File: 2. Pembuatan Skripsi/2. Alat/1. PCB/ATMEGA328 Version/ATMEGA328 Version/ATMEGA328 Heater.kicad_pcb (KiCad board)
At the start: 2 copper layers, 52.3 x 63.6 mm, 64 parts, among them J1 Conn_01x02, J2 Sensors, J3 Screw_Terminal_01x02, J5 FTDI, J6 Conn_02x04_Top_Bottom, K1 EE2-4.5NU, Q1 S9013, Q2 S9013, Q3 S9013, Q4 MMBT2222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

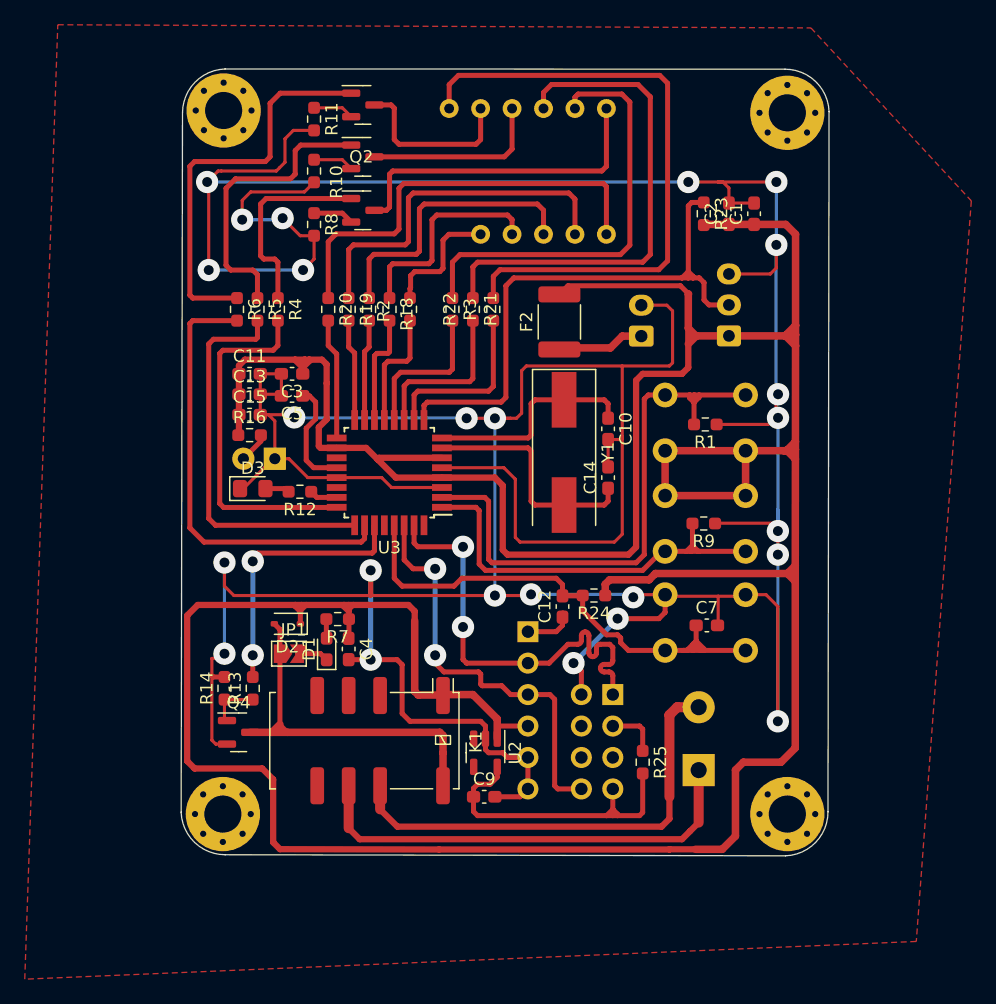
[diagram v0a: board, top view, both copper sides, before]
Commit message: Huge update for ATMEGA328P Board
Program is fully working:

- Get parameter, sensor data, led status, relay status.
- Show parameter on SevSeg
- Connected to NodeRed
- Board design is revised based on actual board
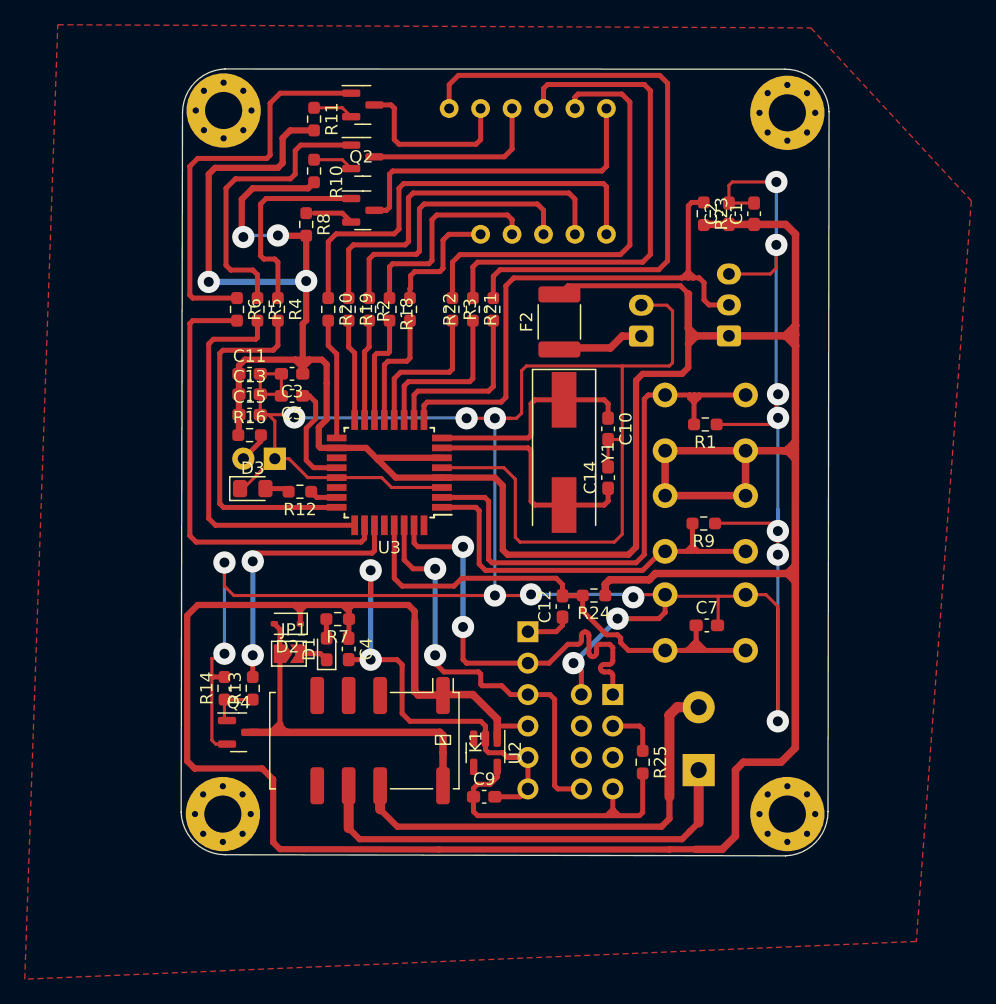
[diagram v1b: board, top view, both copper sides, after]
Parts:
- R10, R8: value 100 -> 1K
- R11: value 100 -> 1k
- R17, R18, R19, R20, R21, R22, R3: value 1K -> 510
- R23: value 10K -> 4K7
- moved R8 0.63 mm to (64.5, 75.6)
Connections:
- R10 pad 2: GND -> VCC
- R11 pad 2: GND -> VCC
- R5 pad 1: Net-(Q2-B) -> EN2
- R5 pad 2: EN2 -> Net-(Q2-B)
- R8 pad 2: GND -> VCC
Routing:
- net GND: track 411.5 -> 324.8 mm, vias 25 -> 19
- net VCC: track 321.0 -> 373.7 mm, vias 0 -> 4
